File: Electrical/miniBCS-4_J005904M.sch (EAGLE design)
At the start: 173 parts, among them IC1 WIZ850io, J11 QWIIC_RIGHT_ANGLE, J14 A0/A1, J2 1734035-2, M2 TEENSY4.1, U1 ADA4084, U10 MAX11300GCM, U11 CAT811, U2 2G17, U3 ISL23425, U4 AD9833, U5 ISO1H815G, U6 78L12, U7 ADM3312/5, U8 2G17, U9 79L12, X1 OSC-OE-CFPS-9

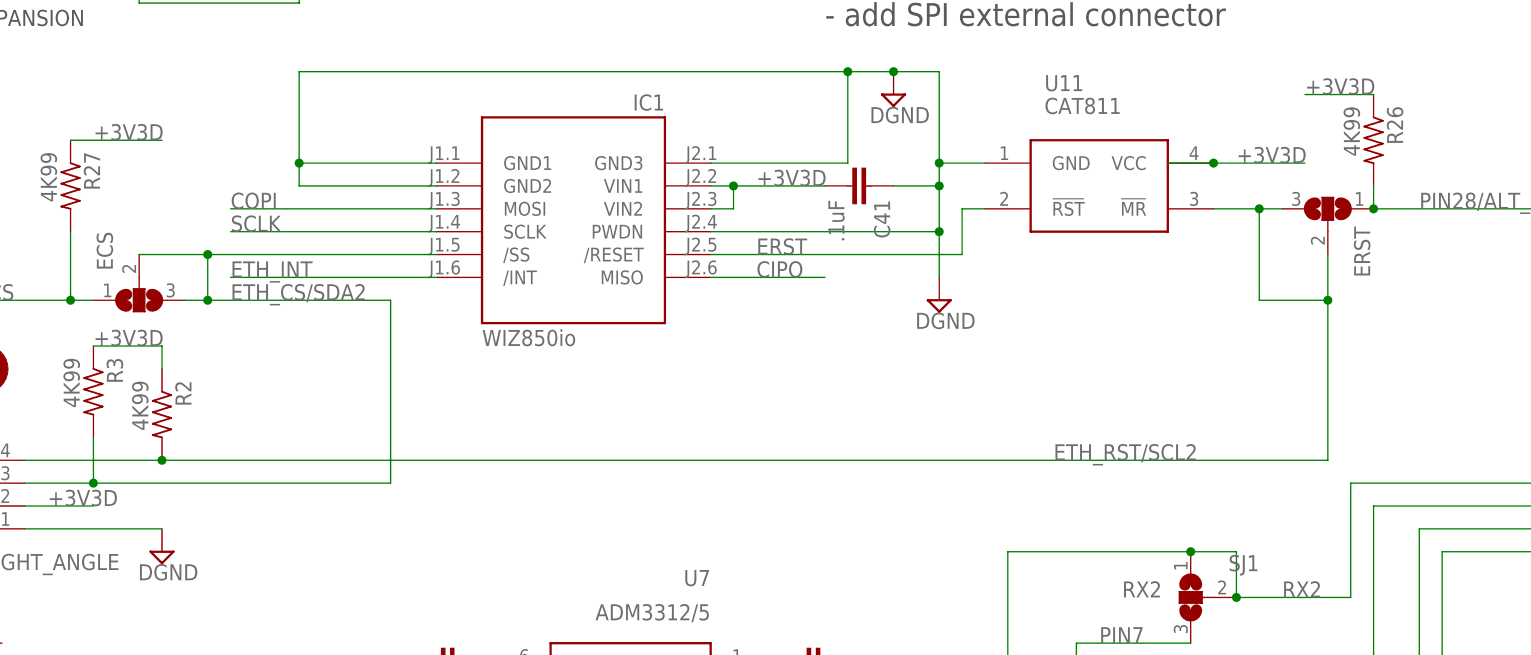
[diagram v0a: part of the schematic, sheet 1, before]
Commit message: Updated BOM, PCB files, example, and laser cut file
Add QWIIC and SPI connector cutouts to laser file
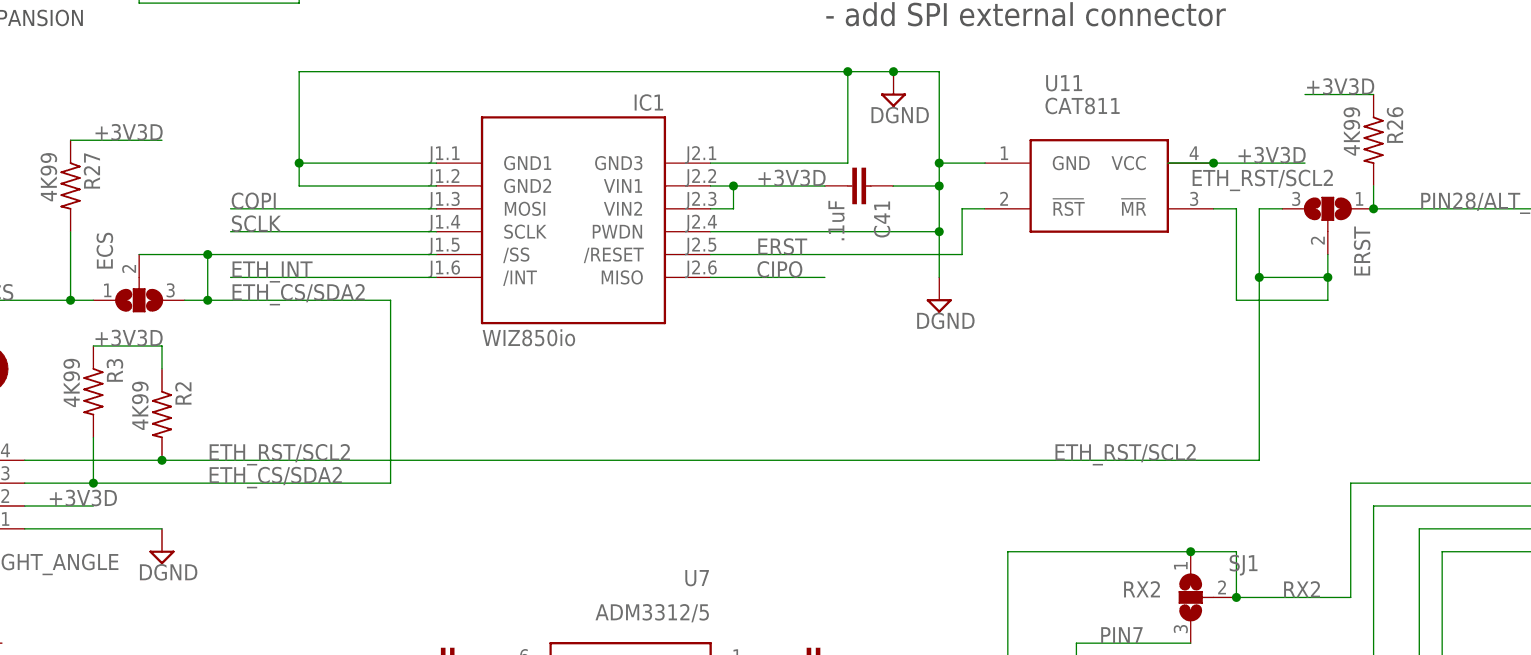
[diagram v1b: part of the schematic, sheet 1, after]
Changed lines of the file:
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@@
 <pinref part="J11" gate="J1" pin="4"/>
 <wire x1="-177.8" y1="243.84" x2="-162.56" y2="243.84" width="0.1524" layer="91"/>
-<wire x1="-162.56" y1="243.84" x2="-33.02" y2="243.84" width="0.1524" layer="91"/>
+<wire x1="-162.56" y1="243.84" x2="-40.64" y2="243.84" width="0.1524" layer="91"/>
 <pinref part="R2" gate="G$1" pin="2"/>
 <junction x="-162.56" y="243.84"/>
@@
 <wire x1="-38.1" y1="271.78" x2="-40.64" y2="271.78" width="0.1524" layer="91"/>
 <pinref part="ERST" gate="G$1" pin="2"/>
-<wire x1="-33.02" y1="266.7" x2="-33.02" y2="261.62" width="0.1524" layer="91"/>
-<wire x1="-33.02" y1="261.62" x2="-40.64" y2="261.62" width="0.1524" layer="91"/>
-<wire x1="-40.64" y1="261.62" x2="-40.64" y2="271.78" width="0.1524" layer="91"/>
-<junction x="-40.64" y="271.78"/>
+<wire x1="-33.02" y1="266.7" x2="-33.02" y2="264.16" width="0.1524" layer="91"/>
+<wire x1="-33.02" y1="264.16" x2="-40.64" y2="264.16" width="0.1524" layer="91"/>
+<wire x1="-40.64" y1="264.16" x2="-40.64" y2="271.78" width="0.1524" layer="91"/>
 <pinref part="U11" gate="G$1" pin="!MR"/>
-<wire x1="-45.72" y1="271.78" x2="-40.64" y2="271.78" width="0.1524" layer="91"/>
+<wire x1="-45.72" y1="271.78" x2="-43.18" y2="271.78" width="0.1524" layer="91"/>
 <label x="-63.5" y="243.84" size="1.778" layer="95"/>
-<wire x1="-33.02" y1="243.84" x2="-33.02" y2="261.62" width="0.1524" layer="91"/>
-<junction x="-33.02" y="261.62"/>
+<junction x="-33.02" y="264.16"/>
+<label x="-157.48" y="243.84" size="1.778" layer="95"/>
+<label x="-48.26" y="274.32" size="1.778" layer="95"/>
+<wire x1="-33.02" y1="261.62" x2="-33.02" y2="264.16" width="0.1524" layer="91"/>
+<wire x1="-43.18" y1="271.78" x2="-43.18" y2="261.62" width="0.1524" layer="91"/>
+<wire x1="-43.18" y1="261.62" x2="-33.02" y2="261.62" width="0.1524" layer="91"/>
+<wire x1="-40.64" y1="264.16" x2="-40.64" y2="243.84" width="0.1524" layer="91"/>
+<junction x="-40.64" y="264.16"/>
 </segment>
 <segment>
@@
 <wire x1="-170.18" y1="246.38" x2="-170.18" y2="241.3" width="0.1524" layer="91"/>
 <junction x="-170.18" y="241.3"/>
+<label x="-157.48" y="241.3" size="1.778" layer="95"/>
 </segment>
 <segment>
